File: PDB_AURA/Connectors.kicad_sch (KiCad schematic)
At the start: 19 parts, among them J200 532617010, J201 XT30PW-F, J202 XT30PW-F, J203 XT30PW-F, J204 XT30PW-F, Q200 HSK10N06, Q201 HSK10N06, U200 LTV-217-B-G, U201 LTV-217-B-G, U202 INA219AIDCNR

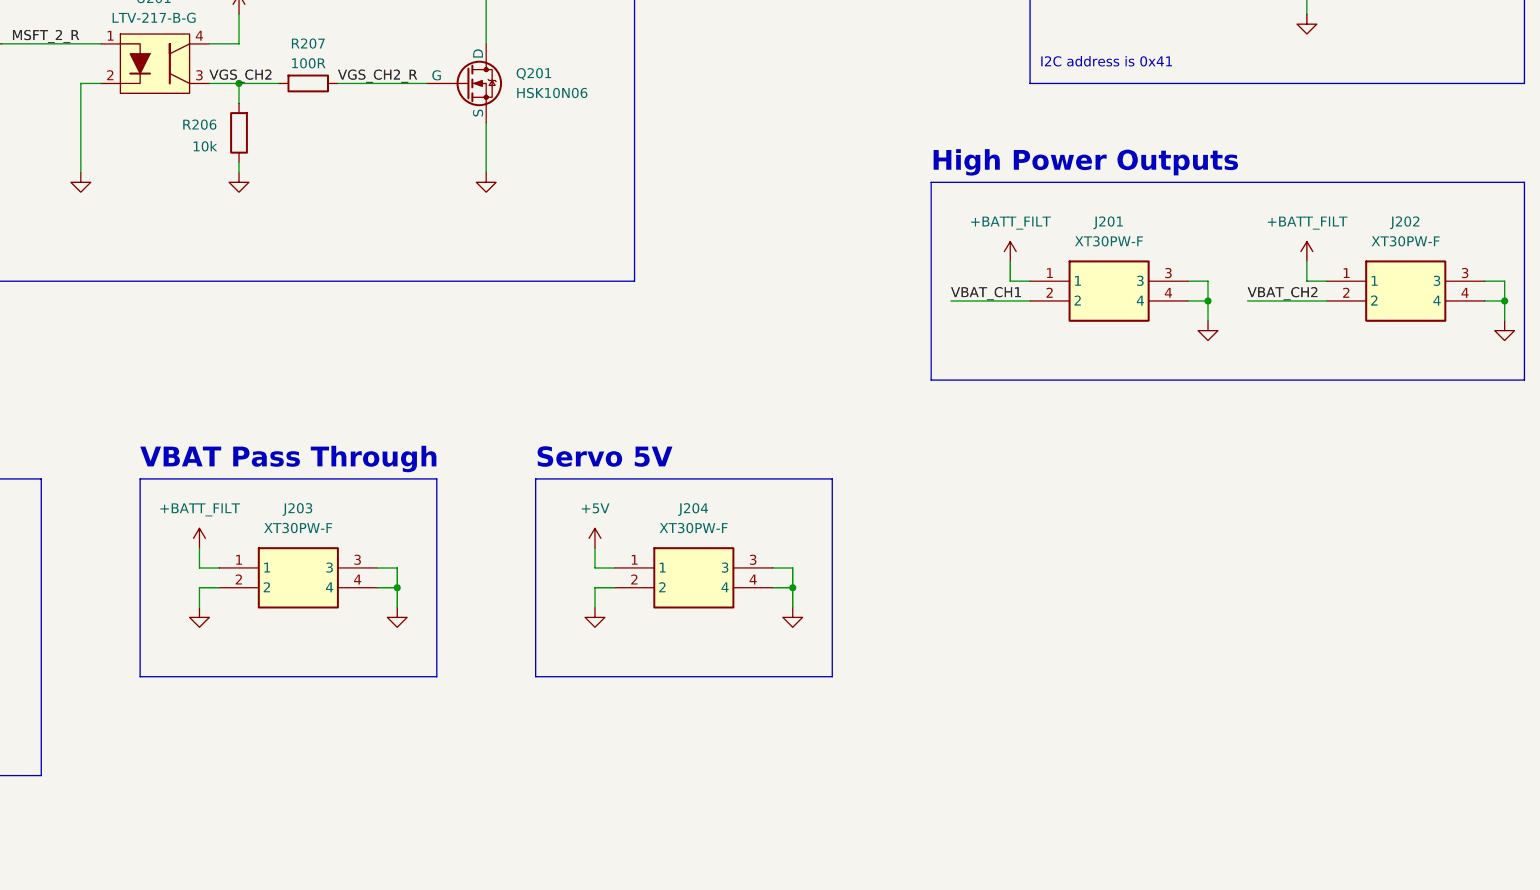
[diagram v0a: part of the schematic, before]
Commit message: New PDB specs chosen
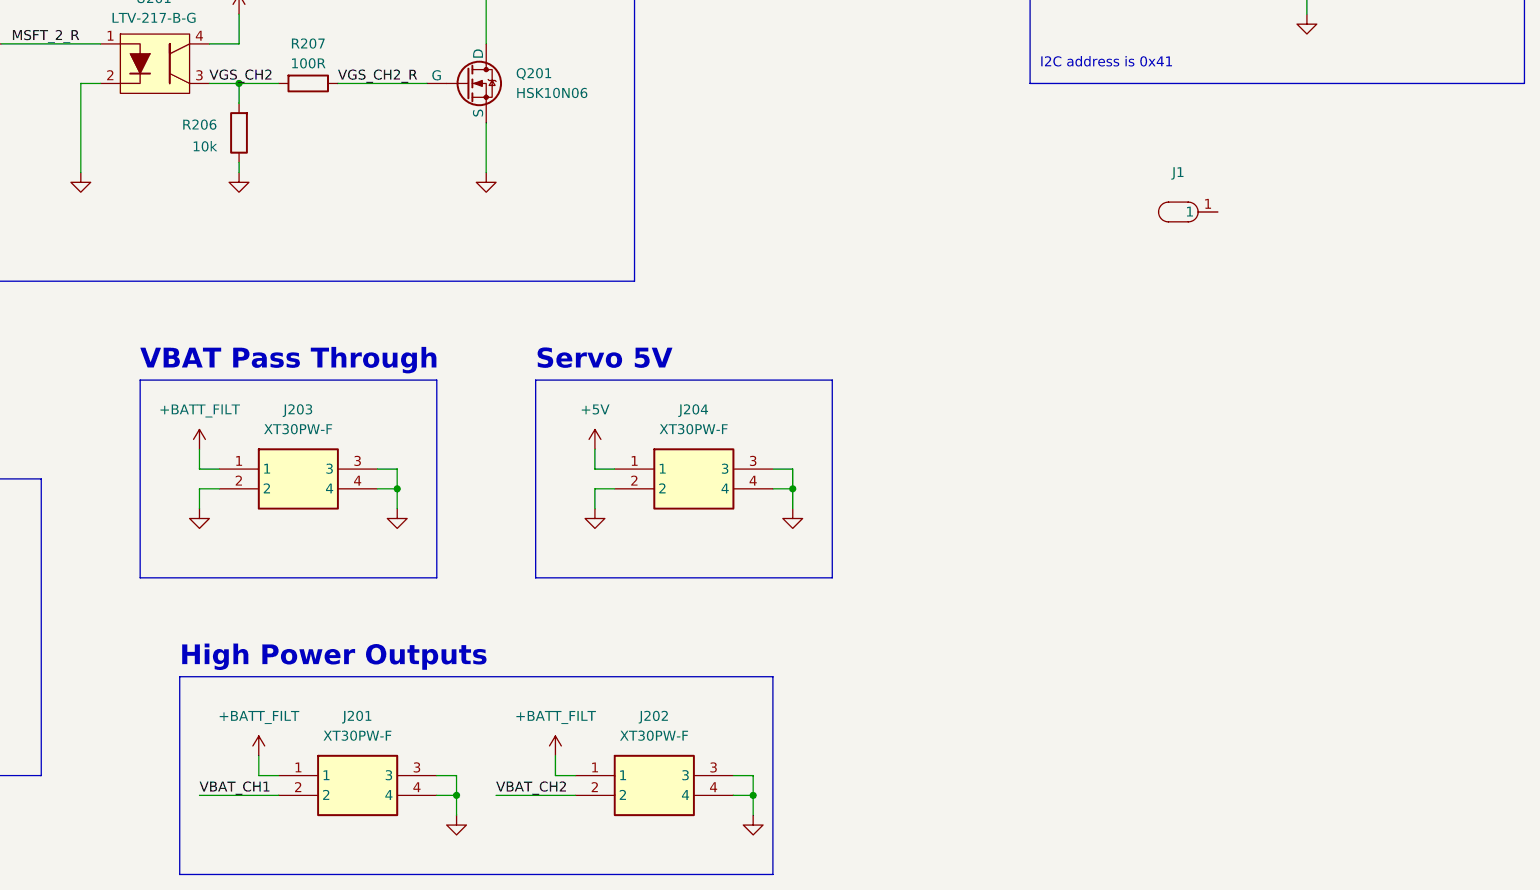
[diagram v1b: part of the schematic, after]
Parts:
- added J1: ~, SOLDER_PAD:PWR_SOLDER_PAD, symbol SOLDER_PAD:Power_Solder_Pad
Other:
- moved on the sheet: J201, J202, J203, J204

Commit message: Moving to laptop
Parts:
- added D3: D, SBR3M30P17:SBR3M30P17, symbol Device:D
- added J2, J3, J4, J5, J6, J7, J8: ~, SOLDER_PAD:PWR_SOLDER_PAD, symbol SOLDER_PAD:Power_Solder_Pad
- R201, R205: value 470R -> 220R
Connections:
- net +BATT_FILT: now also J1.1, J3.1, J5.1, J7.1
- net GND: now also J2.1, J4.1, J6.1, J8.1
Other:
- moved on the sheet: J1

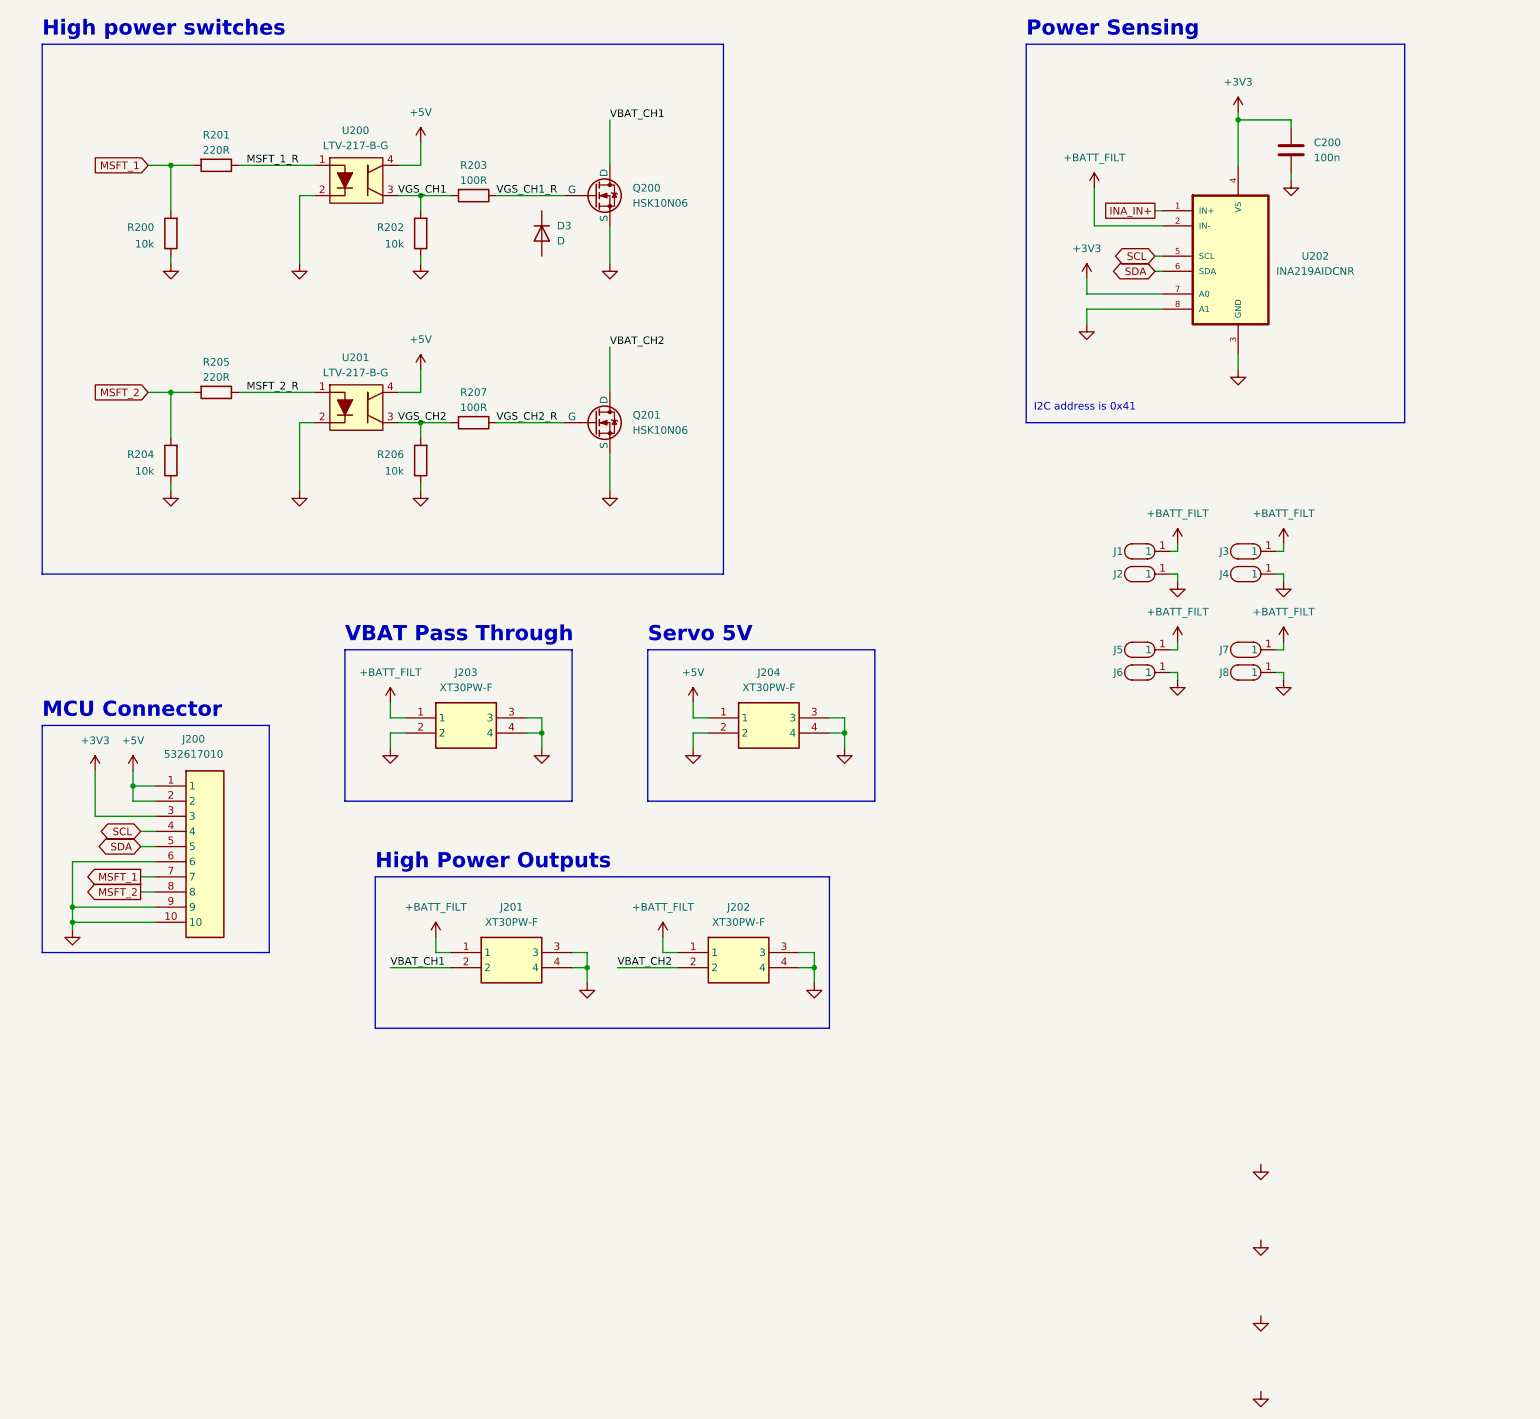
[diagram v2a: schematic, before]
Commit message: Annotated schematic for PDB
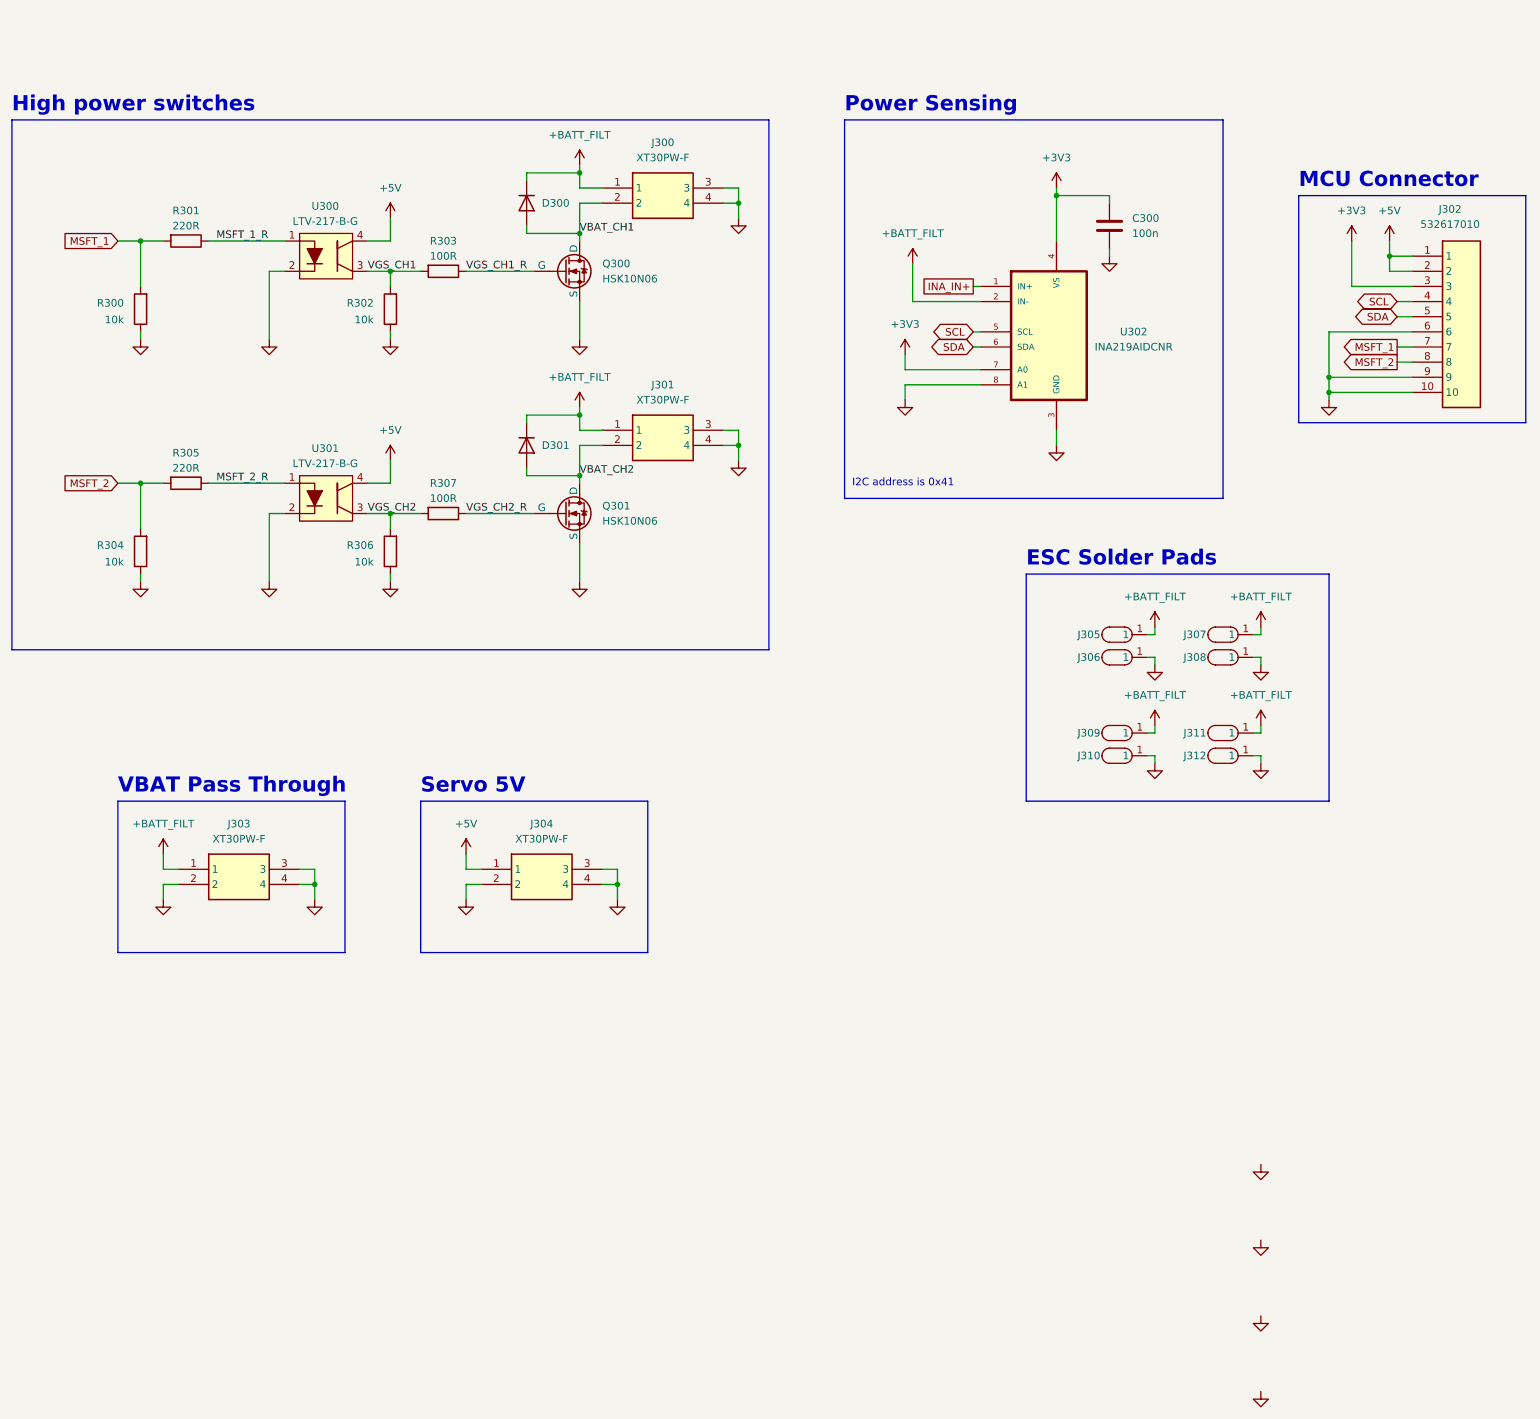
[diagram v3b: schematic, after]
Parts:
- removed J202: XT30PW-F, XT30PWF:XT30PWF, symbol XT30PW-F:XT30PW-F
- added D301: SBR3M30P17, SBR3M30P17:SBR3M30P17, symbol Device:D
- added J301: XT30PW-F, XT30PWF:XT30PWF, symbol XT30PW-F:XT30PW-F
- D300: renamed from D3; value D -> SBR3M30P17
- renumbered C200 to C300, J201 to J300, J200 to J302, J203 to J303, J204 to J304, J1 to J305, J2 to J306, J3 to J307, J4 to J308, J5 to J309, J6 to J310, J7 to J311, J8 to J312, Q200 to Q300, Q201 to Q301, R200 to R300, R201 to R301, R202 to R302, R203 to R303, R204 to R304, R205 to R305, R206 to R306, R207 to R307, U200 to U300, U201 to U301, U202 to U302
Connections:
- net +BATT_FILT: now also D300.1 (K), D301.1 (K), J301.1
- net GND: now also J301.3, J301.4
- net VBAT_CH1: now also D300.2 (A)
- net VBAT_CH2: now also D301.2 (A), J301.2
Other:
- note added: "ESC Solder Pads"
- note removed: "High Power Outputs"
- title: Actuator Outputs -> Connectors and Outputs
- moved on the sheet: C300, D300, J300, J302, J303, J304, J305, J306, J307, J308, J309, J310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

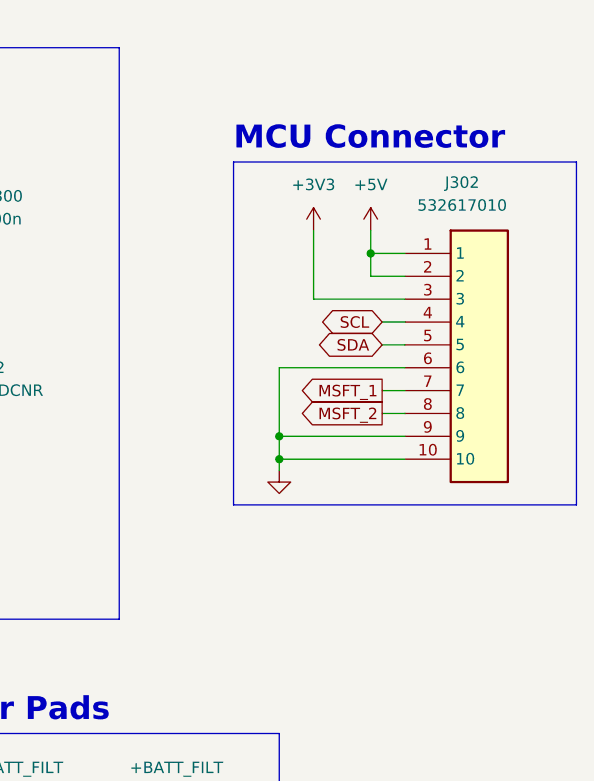
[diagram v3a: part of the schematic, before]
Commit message: Second Layout Attempt
Renamed all components and placed them all.
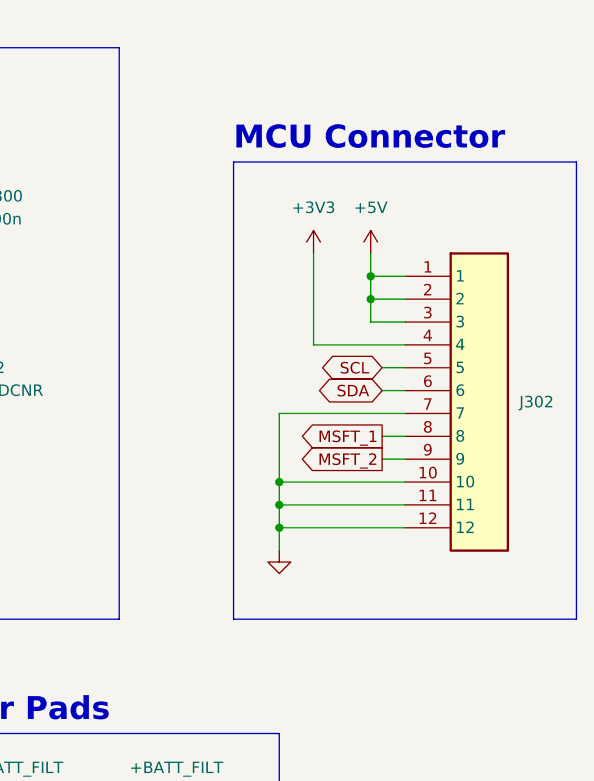
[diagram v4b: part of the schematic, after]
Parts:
- removed J302: 532617010, 532617010:532617010, symbol 532617010:532617010
- added J302: 532617012, 532611271:53261-1271, symbol 532617012:532617012
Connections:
- net +3V3: now also J302.4
- net +5V: now also J302.1, J302.2, J302.3
- net GND: now also J302.10, J302.11, J302.12, J302.7
- net MSFT_1: now also J302.8
- net MSFT_2: now also J302.9
- net SCL: now also J302.5
- net SDA: now also J302.6

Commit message: Continued Routing
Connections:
- net +5V: now also J302.10, J302.11, J302.12; no longer J302.1, J302.2, J302.3
- net +BATT_FILT: now also J303.3
- net GND: now also J302.1, J302.2, J302.3; no longer J302.10, J302.11, J302.12, J303.3
- net SCL: now also J302.6; no longer J302.5
- net SDA: now also J302.5; no longer J302.6
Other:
- moved on the sheet: J302, J303

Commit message: Replaced JTAG with Flash
JTAG is used through USB so a Flash chip was added to MCU. PDB is just being cleaned up currently.
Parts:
- C300: footprint Capacitor_SMD:C_0603_1608Metric -> Capacitor_SMD:C_0402_1005Metric
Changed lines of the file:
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@@
 			)
 		)
-		(property "Footprint" "Capacitor_SMD:C_0603_1608Metric"
+		(property "Footprint" "Capacitor_SMD:C_0402_1005Metric"
 			(at 205.4352 59.69 0)
 			(effects
